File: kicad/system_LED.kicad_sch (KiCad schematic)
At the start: 1 part

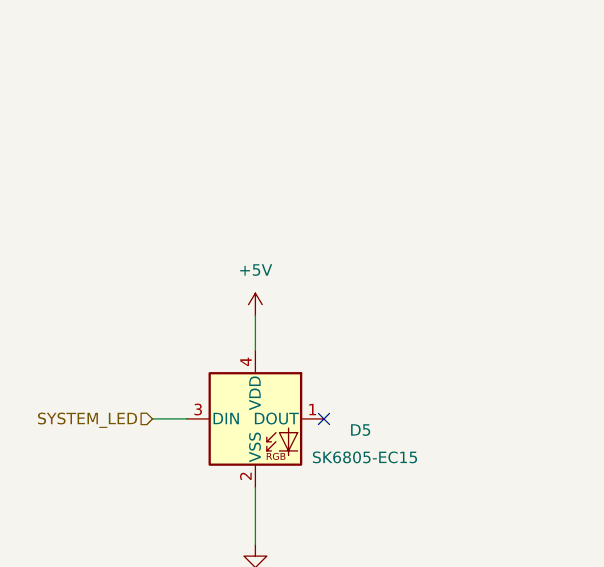
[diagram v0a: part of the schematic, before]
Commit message: feat: remake power management and use the same as the reference DK
Signed-off-by: Bobo Bäck Engström <bobo@id8-engineering.io>
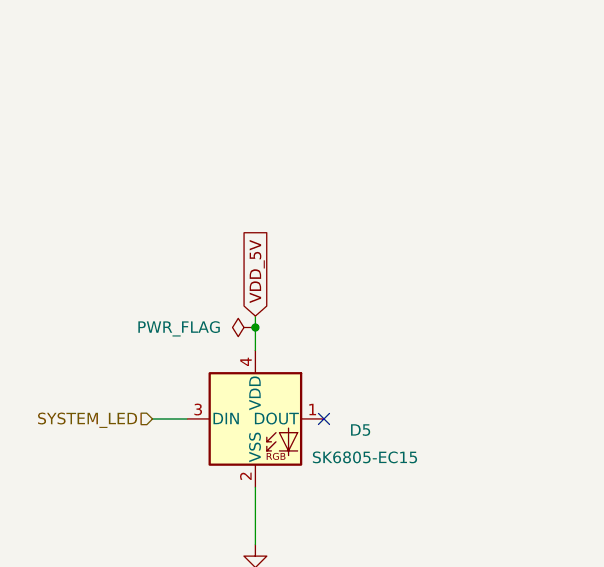
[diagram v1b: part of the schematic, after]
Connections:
- net +5V renamed VDD_5V
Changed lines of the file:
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@@
 		)
+	)
+	(junction
+		(at 93.98 74.93)
+		(diameter 0)
+		(color 0 0 0 0)
 	)
 	(no_connect
@@
 	(wire
 		(pts
-			(xy 93.98 73.66) (xy 93.98 77.47)
+			(xy 93.98 73.66) (xy 93.98 74.93)
 		)
 		(stroke
@@
 		(pts
 			(xy 93.98 99.06) (xy 93.98 92.71)
+		)
+		(stroke
+			(width 0)
+			(type default)
+		)
+	)
+	(wire
+		(pts
+			(xy 93.98 74.93) (xy 93.98 77.47)
 		)
 		(stroke
@@
 		)
 	)
+	(global_label "VDD_5V"
+		(shape input)
+		(at 93.98 73.66 90)
+		(fields_autoplaced yes)
+		(effects
+			(font
+				(size 1.27 1.27)
+			)
+			(justify left)
+		)
+		(property "Intersheetrefs" "${INTERSHEET_REFS}"
+			(at 93.98 63.7805 90)
+			(effects
+				(font
+					(size 1.27 1.27)
+				)
+				(justify left)
+				(hide yes)
+			)
+		)
+	)
 	(hierarchical_label "SYSTEM_LED"
 		(shape input)
@@
 	)
 	(symbol
-		(lib_id "seven_lib:+5V")
-		(at 93.98 73.66 0)
+		(lib_id "seven_lib:PWR_FLAG")
+		(at 93.98 74.93 90)
 		(unit 1)
 		(exclude_from_sim no)
@@
 		(dnp no)
 		(fields_autoplaced yes)
-		(property "Reference" "#PWR048"
-			(at 93.98 77.47 0)
-			(effects
-				(font
-					(size 1.27 1.27)
-				)
-				(hide yes)
-			)
-		)
-		(property "Value" "+5V"
-			(at 93.98 68.58 0)
-			(effects
-				(font
-					(size 1.27 1.27)
-				)
+		(property "Reference" "#FLG02"
+			(at 92.075 74.93 0)
+			(effects
+				(font
+					(size 1.27 1.27)
+				)
+				(hide yes)
+			)
+		)
+		(property "Value" "PWR_FLAG"
+			(at 90.17 74.9299 90)
+			(effects
+				(font
+					(size 1.27 1.27)
+				)
+				(justify left)
 			)
 		)
 		(property "Footprint" ""
-			(at 93.98 73.66 0)
-			(effects
-				(font
-					(size 1.27 1.27)
-				)
-				(hide yes)
-			)
-		)
-		(property "Datasheet" ""
-			(at 93.98 73.66 0)
-			(effects
-				(font
-					(size 1.27 1.27)
-				)
-				(hide yes)
-			)
-		)
-		(property "Description" "Power symbol creates a global label with name \"+5V\""
-			(at 93.98 73.66 0)
+			(at 93.98 74.93 0)
+			(effects
+				(font
+					(size 1.27 1.27)
+				)
+				(hide yes)
+			)
+		)
+		(property "Datasheet" "~"
+			(at 93.98 74.93 0)
+			(effects
+				(font
+					(size 1.27 1.27)
+				)
+				(hide yes)
+			)
+		)
+		(property "Description" "Special symbol for telling ERC where power comes from"
+			(at 93.98 74.93 0)
 			(effects
 				(font
@@
 		)
 		(instances
-			(project "seven"
+			(project ""
 				(path "/8e3cc843-5797-49f3-8b3a-1c11450ccd1e/57402695-b5b6-411c-ba67-6244479e2395"
-					(reference "#PWR048")
+					(reference "#FLG02")
 					(unit 1)
 				)

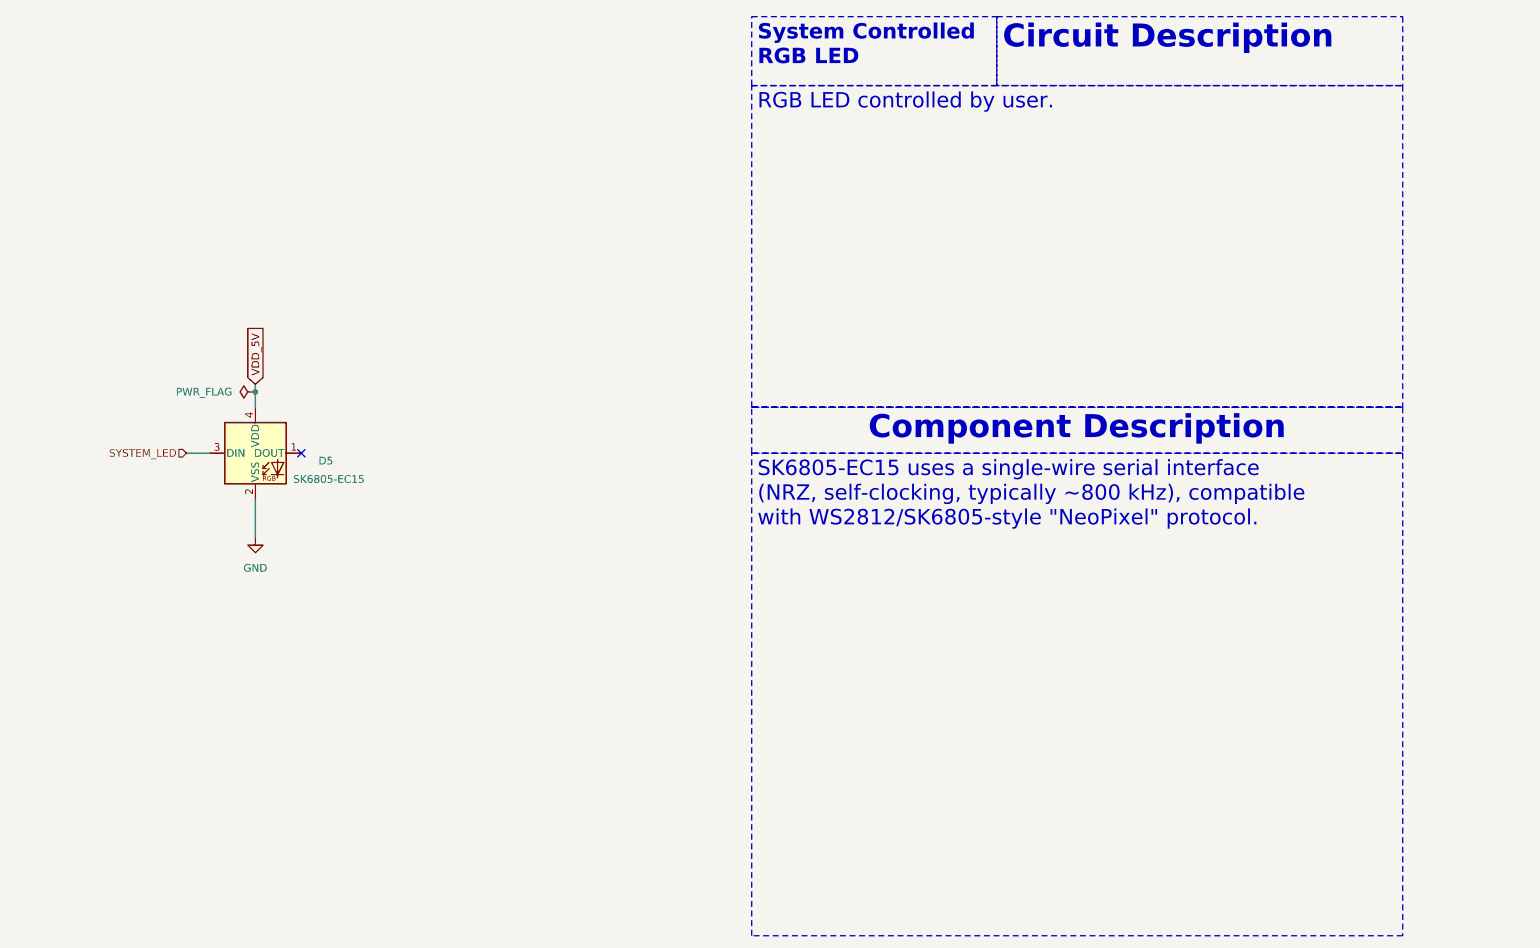
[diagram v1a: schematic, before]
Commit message: docs: update documentation to be more accurate
Signed-off-by: Bobo Bäck Engström <bobo@id8-engineering.io>
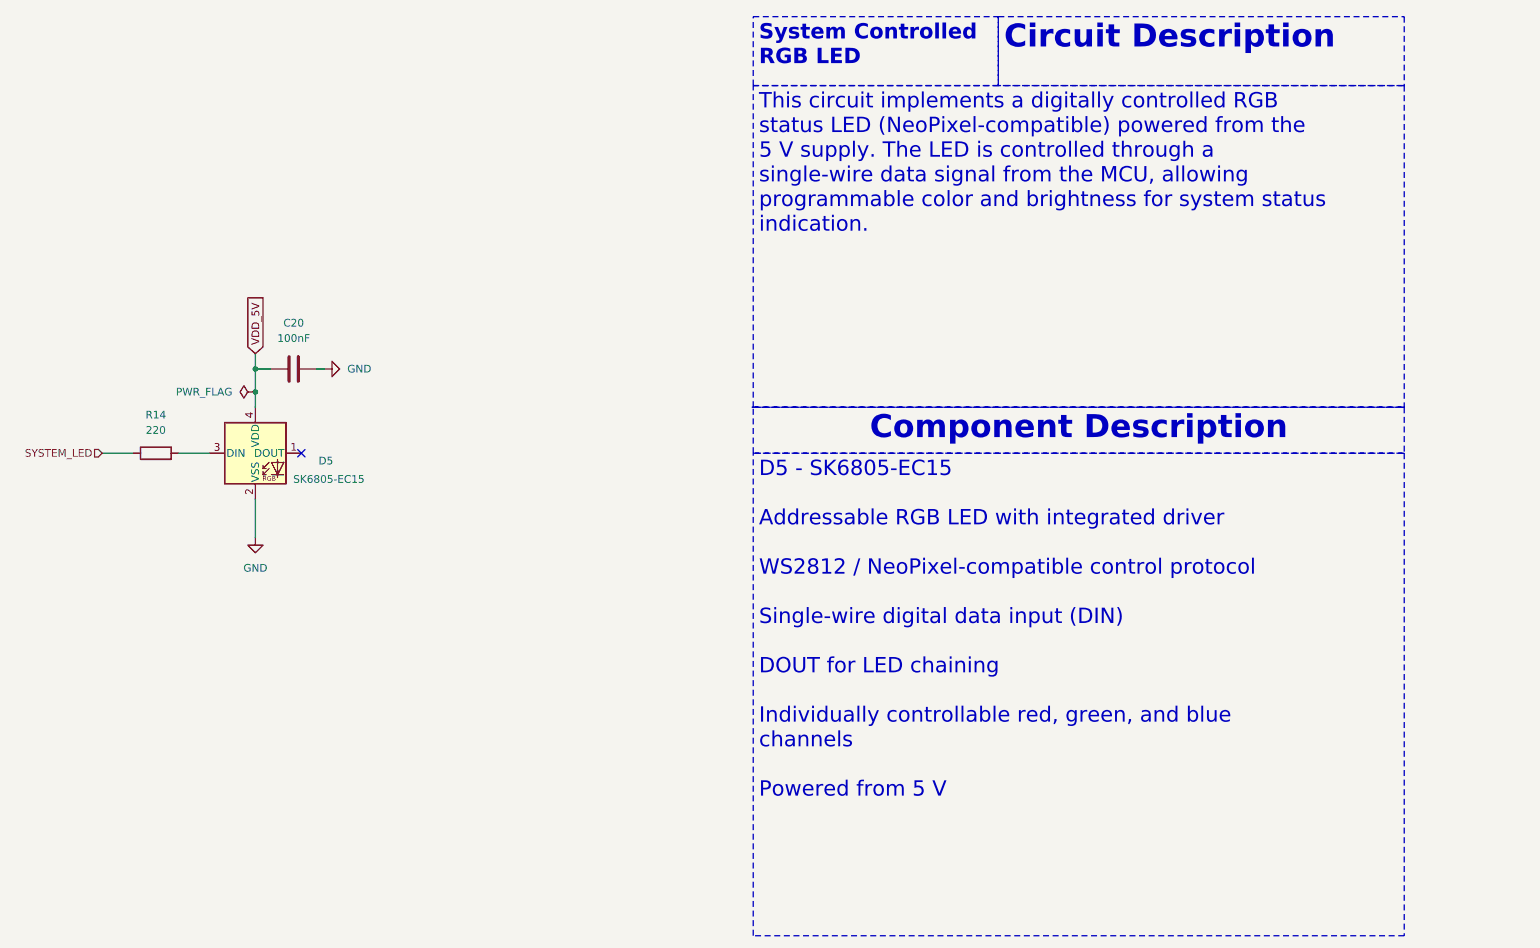
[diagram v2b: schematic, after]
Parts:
- added C20: 100nF, seven-lib:C_1812_4532Metric, symbol seven_lib:C
- added R14: 220, seven-lib:R_0603_1608Metric, symbol seven_lib:R
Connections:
- net GND: now also C20.2
- net SYSTEM_LED: now also R14.1; no longer D5.3 (DIN)
- net VDD_5V: now also C20.1
- new net: D5.3 (DIN), R14.2
